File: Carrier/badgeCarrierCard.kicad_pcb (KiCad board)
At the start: 4 copper layers, 90 x 145 mm, 158 parts, among them J1 USB_C_Receptacle_USB2.0_16P, J2 MDT420M02003, J3 Conn_01x08, J5 SMA-J-P-X-RA-TH1, J6 1-1734248-5, J7 Conn_01x10, J8 USB_C_Receptacle_USB2.0_16P, J9 Conn_01x30, M1 Z30C1T8460001, Q1 AO3400A, Q2 AO3400A, Q3 AO3400A, Q4 BC847, U1 TCA8418, U10 EL817S1C, U10 JDJELECTRONICS_2023_LOGO, U11 TPSGM7227YUWQ10G, U12 USBLC6-2SC6, U15 AP3032, U16 AP3032, U2 IP5306, U3 AMS1117-1.8, U4 ESP32-C6-WROOM-1, U5 Ai-Thinker-Ra-01H, U6 MAX98357A, U7 BME680, U8 BMI270, U9 EL817S1C, U9 JDJELECTRONICS_2023_LOGO

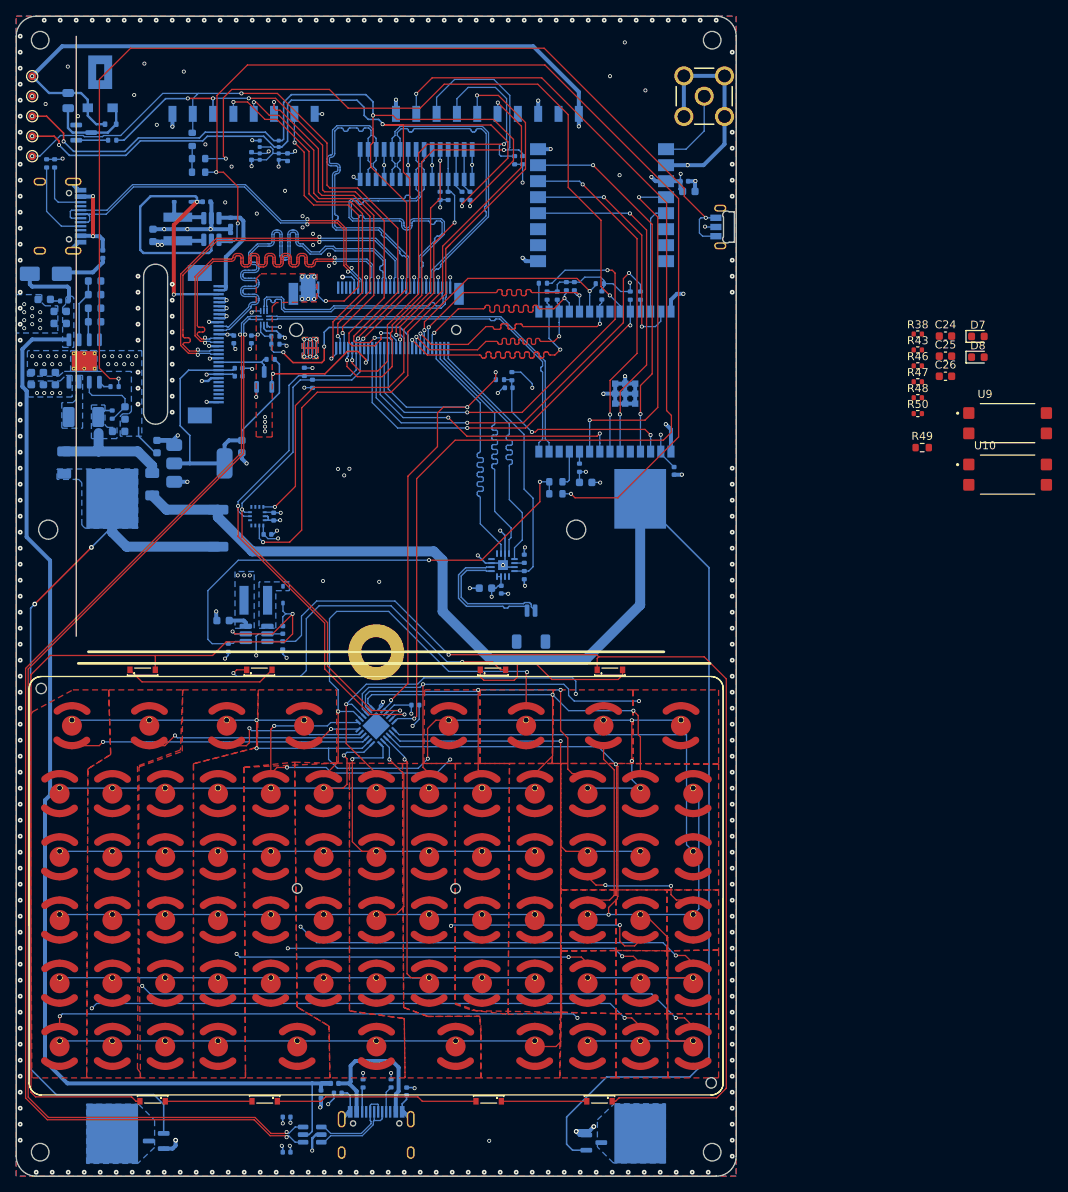
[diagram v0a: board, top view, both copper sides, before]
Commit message: fix: implement balancer changes
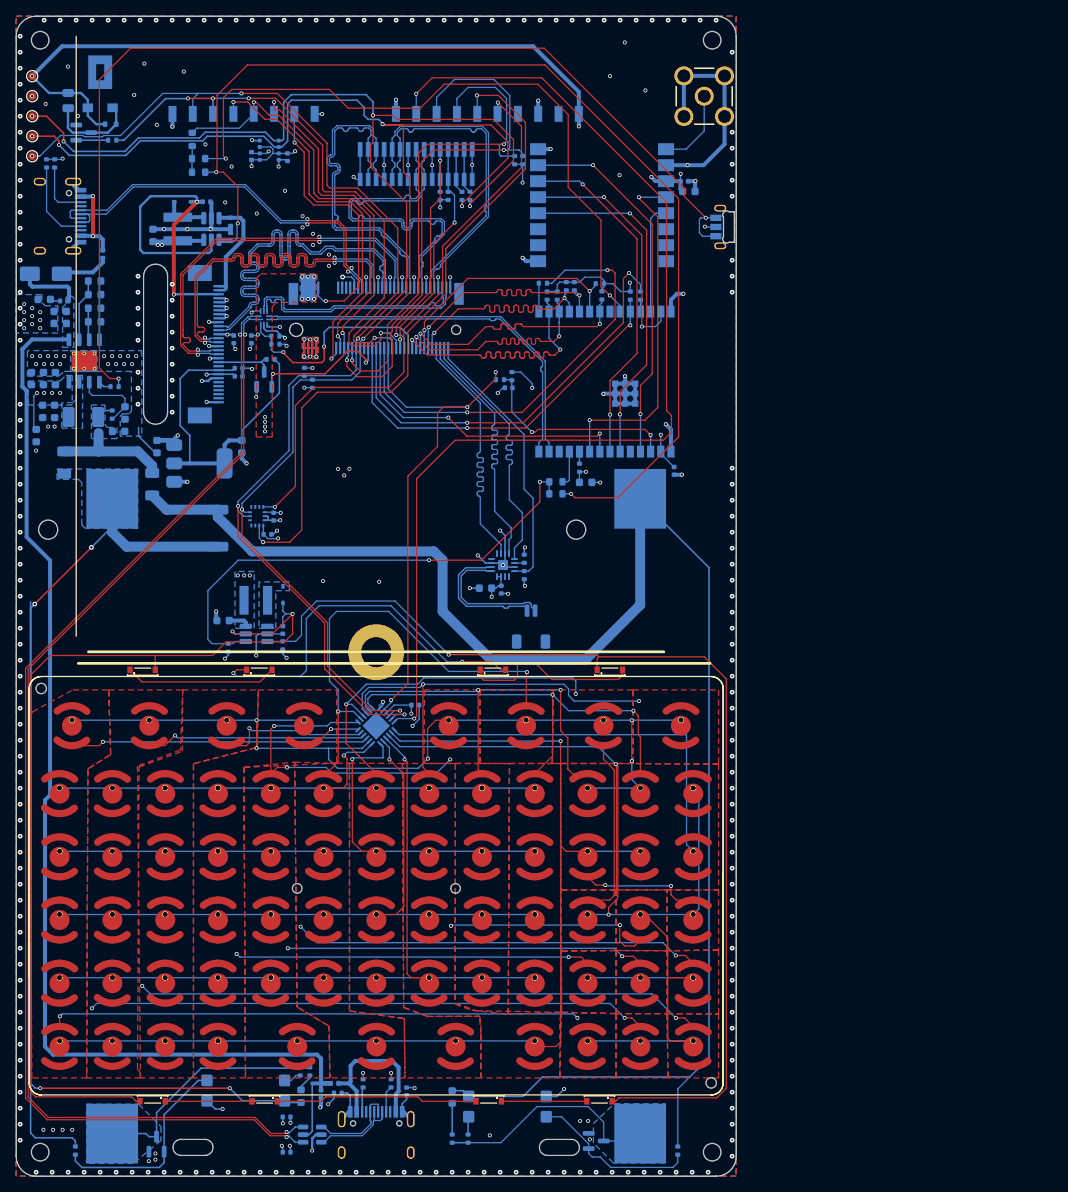
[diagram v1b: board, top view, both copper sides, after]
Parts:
- removed C26: 22uF, Capacitor_SMD:C_0603_1608Metric
- removed R49: 0R, Resistor_SMD:R_0603_1608Metric
- removed R50: 470, Resistor_SMD:R_0402_1005Metric
- removed the U9 at (153.9, 80.9)
- removed the U9 at (38.8, 173.8)
- added C23: 22uF, Capacitor_SMD:C_0603_1608Metric, B.Cu at (32.5, 82.4)
- added R40: 470, Resistor_SMD:R_0402_1005Metric, B.Cu at (66.7, 161.9)
- added U9: EL817S1C, EL817:SOIC254P1030X390-4N, B.Cu at (91.4, 166.3)
- C24, C25, D7, D8, R38, R43, R46, R47, R48, U10: moved to B.Cu
- moved R43 145.3 mm to (37.4, 171.8), turned to 90 degrees
- moved D7 127.2 mm to (65.6, 165.0), turned to 90 degrees
- moved U10 122.5 mm to (58.7, 164.3), turned to 180 degrees
- moved R38 120.2 mm to (65.5, 161.9), turned to 90 degrees
- moved D8 113.5 mm to (84.5, 165.1), turned to -90 degrees
- moved C24 113.3 mm to (33.3, 79.4), turned to -90 degrees
- moved R46 112.8 mm to (84.5, 170.3), turned to -90 degrees
- moved C25 111.6 mm to (34.8, 79.4), turned to -90 degrees
- moved R47 110.0 mm to (86.5, 170.3), turned to -90 degrees
- moved R48 98.8 mm to (112.7, 171.8), turned to 90 degrees
- moved Q1 0.40 mm to (47.5, 171.0), turned to 90 degrees
- moved Q3 0.36 mm to (102.5, 170.6)
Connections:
- D7 pad 2: Net-(D7-A) (its old number) -> Net-(D6-A)
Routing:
- net Net-(BT1-+): track 120.6 -> 206.4 mm, vias 2 -> 4
- net /GPIO4: track 0.00 -> 84.5 mm, vias 0 -> 3
- net /GPIO1: track 130.2 -> 52.0 mm, vias 5 -> 2
- net /GPIO3: track 0.00 -> 72.5 mm, vias 0 -> 4
- net (no net): track 72.9 -> 0.42 mm, vias 4 -> 0
- net Net-(BT1--): track 0.00 -> 30.3 mm
- net Net-(BT2--): track 0.00 -> 28.9 mm
- net Net-(Q1-G): track 0.00 -> 25.6 mm
- net Net-(Q3-G): track 0.00 -> 21.0 mm
- net Net-(BT2-+): track 190.3 -> 207.0 mm
- net +5V: track 160.4 -> 165.3 mm
- net Net-(D7-A): track 0.00 -> 3.90 mm
- net Net-(D6-A): track 11.4 -> 13.7 mm
- net Net-(R47-Pad1): track 0.00 -> 2.25 mm
- net Net-(R35-Pad1): track 0.00 -> 2.21 mm
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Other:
- outline, holes or cut-outs redrawn

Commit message: push final
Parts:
- removed the U10 at (111.6, 34.0)
- added R49: 0R, Resistor_SMD:R_0402_1005Metric, B.Cu at (42.0, 46.6)
- renumbered C23 to C26, R40 to R50
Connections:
- D7 pad 2: Net-(D6-A) -> Net-(D7-A)
- R50 pad 1: Net-(D6-A) -> Net-(D7-A)
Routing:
- net Net-(D6-A): track 13.7 -> 11.4 mm
- net Net-(D7-A): track 0.00 -> 2.26 mm
- net /Vibrator/PWM_VIB: track 0.00 -> 1.52 mm
- net /GPIO3: track 72.5 -> 73.4 mm
- net GND: track 204.5 -> 204.4 mm, vias 359 -> 376
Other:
- board text added: "WHY NOT ?"
- board text added: "¯\_(ツ)_/¯"
